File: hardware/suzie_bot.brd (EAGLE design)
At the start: 98.7 x 71.1 mm, 37 parts, among them IC1 LT1529CT33, IC2 L9637D, IC3 IC_TXB0108-TSSOP-20, U1 ATMEGA1284P-AU, Y1 14.7456, Y2 6.0, Y3 16.0

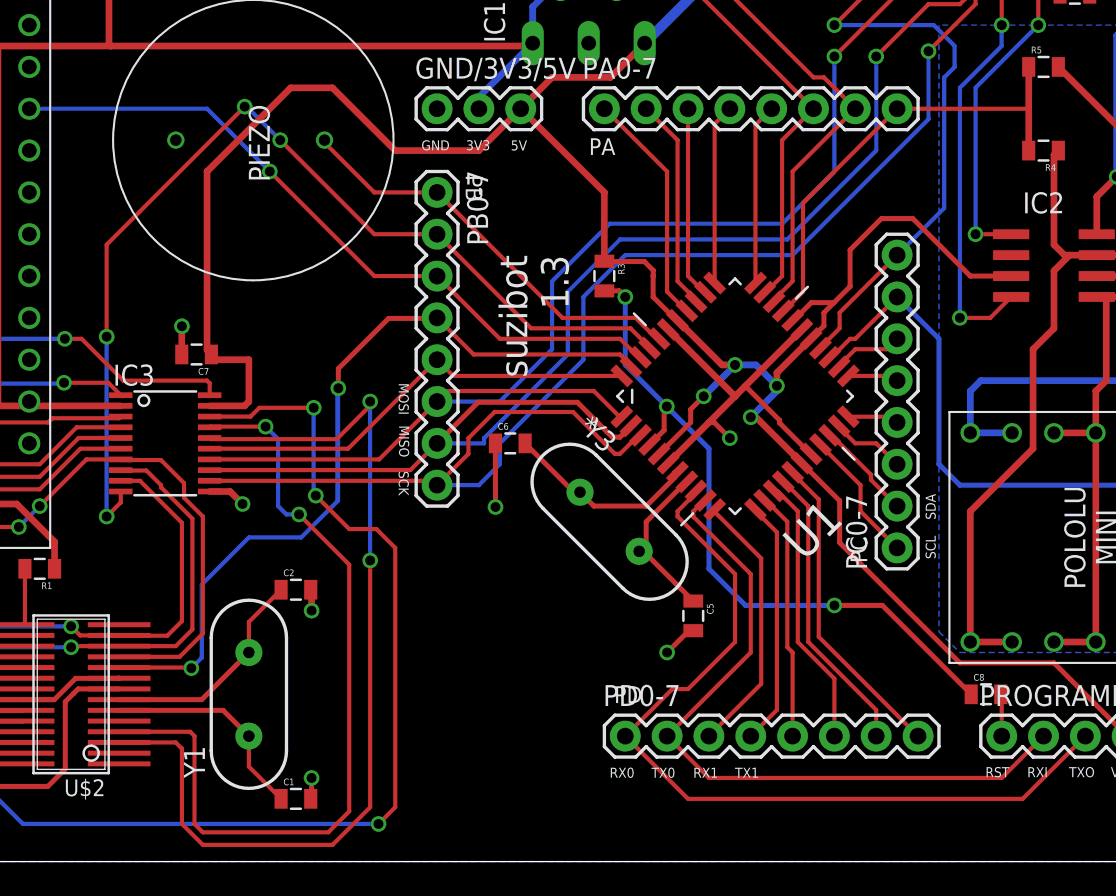
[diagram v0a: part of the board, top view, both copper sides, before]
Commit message: Adding LED to PB1 (per https://www.flickr.com/photos/maniacbug/6413368937/)
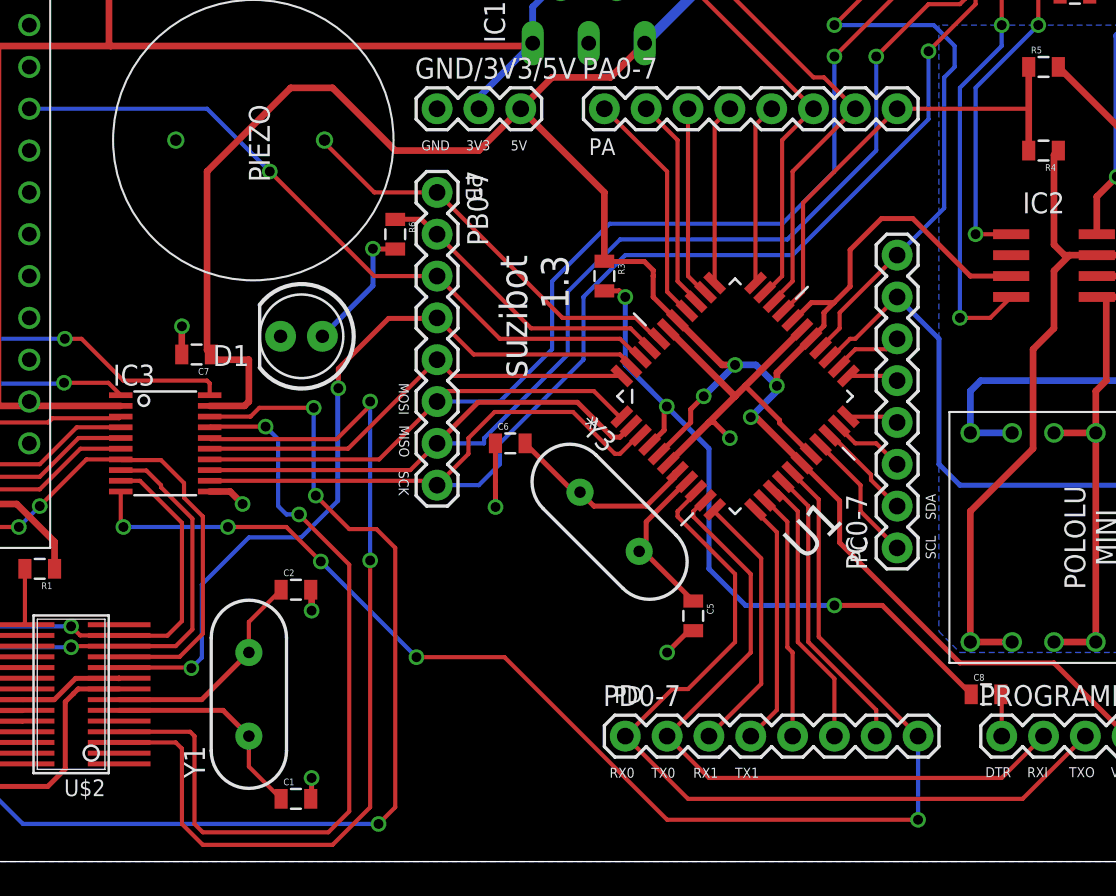
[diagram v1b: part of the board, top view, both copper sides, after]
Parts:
- added D1: RED, SparkFun-LED:LED5MM
- added R6: 330, SparkFun-Passives:0805
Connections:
- removed net PB1: IC3.10, PB0-7.2, U1.41
- new net N$2: PB0-7.2, R6.1, U1.41
- new net N$25: D1.A, R6.2
- net GND: now also D1.K
- net PD7: now also IC3.10
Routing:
- net PD7: track 19.2 -> 82.1 mm, vias 0 -> 5
- net PB1: track 60.9 -> 0.00 mm, vias 4 -> 0
- net N$2: track 0.00 -> 18.7 mm
- net N$25: track 0.00 -> 7.96 mm, vias 0 -> 1
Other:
- board text added: "DTR"
- board text removed: "RST"
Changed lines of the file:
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@@
 <layer number="21" name="tPlace" color="7" fill="1" visible="yes" active="yes"/>
 <layer number="22" name="bPlace" color="7" fill="1" visible="yes" active="yes"/>
-<layer number="23" name="tOrigins" color="15" fill="1" visible="no" active="yes"/>
+<layer number="23" name="tOrigins" color="15" fill="1" visible="yes" active="yes"/>
 <layer number="24" name="bOrigins" color="15" fill="1" visible="no" active="yes"/>
 <layer number="25" name="tNames" color="7" fill="1" visible="no" active="yes"/>
@@
 <text x="60.731259375" y="10.64594375" size="1.016" layer="21" rot="R180">PD</text>
 <text x="96.1071375" y="10.71075" size="1.016" layer="21" rot="R180">PROG</text>
-<text x="81.5558875" y="5.125053125" size="0.6096" layer="21">RST</text>
+<text x="81.5558875" y="5.125053125" size="0.6096" layer="21">DTR</text>
 <text x="84.0958875" y="5.125053125" size="0.6096" layer="21">RXI</text>
 <text x="86.6358875" y="5.125053125" size="0.6096" layer="21">TXO</text>
@@
 <element name="R5" library="SparkFun-Passives" package="0805" value="50k" x="85.09" y="48.26"/>
 <element name="U$1" library="dp_devices.v6" package="CON_MICROSD_HINGED" value="CON_MICROSDHINGED" x="7.62" y="10.16" rot="R270"/>
+<element name="D1" library="SparkFun-LED" package="LED5MM" value="RED" x="40.025459375" y="31.90121875" rot="R180"/>
+<element name="R6" library="SparkFun-Passives" package="0805" value="330" x="45.72" y="38.1" rot="R270"/>
 </elements>
 <signals>
@@
 <wire x1="26.31049375" y1="11.12883125" x2="28.94663125" y2="11.12883125" width="0.3048" layer="1"/>
 <wire x1="28.94663125" y1="11.12883125" x2="28.9528" y2="11.135" width="0.3048" layer="1"/>
+<contactref element="D1" pad="K"/>
 </signal>
 <signal name="3V3" class="1">
@@
 <wire x1="76.2" y1="45.72" x2="84.19" y2="45.72" width="0.254" layer="1"/>
 </signal>
-<signal name="PB1">
-<contactref element="U1" pad="41"/>
-<contactref element="PB0-7" pad="2"/>
-<contactref element="IC3" pad="10"/>
-<wire x1="61.166909375" y1="31.1850625" x2="61.166909375" y2="31.225590625" width="0.254" layer="1"/>
-<wire x1="61.166909375" y1="31.225590625" x2="60.0075" y2="32.385" width="0.254" layer="1"/>
-<wire x1="60.0075" y1="32.385" x2="53.975" y2="32.385" width="0.254" layer="1"/>
-<wire x1="53.975" y1="32.385" x2="48.26" y2="38.1" width="0.254" layer="1"/>
-<wire x1="29.05" y1="22.475" x2="29.05" y2="21.811" width="0.254" layer="1"/>
-<wire x1="29.05" y1="21.811" x2="28.194" y2="20.955" width="0.254" layer="1"/>
-<via x="28.194" y="20.955" extent="1-16" drill="0.6"/>
-<wire x1="28.194" y1="20.955" x2="28.194" y2="31.877" width="0.254" layer="16"/>
-<via x="28.194" y="31.877" extent="1-16" drill="0.6"/>
-<wire x1="28.194" y1="31.877" x2="28.194" y2="37.465" width="0.254" layer="1"/>
-<wire x1="28.194" y1="37.465" x2="36.576" y2="45.847" width="0.254" layer="1"/>
-<via x="36.576" y="45.847" extent="1-16" drill="0.6"/>
-<wire x1="36.576" y1="45.847" x2="36.703" y2="45.847" width="0.254" layer="16"/>
-<wire x1="36.703" y1="45.847" x2="38.735" y2="43.815" width="0.254" layer="16"/>
-<via x="38.735" y="43.815" extent="1-16" drill="0.6"/>
-<wire x1="38.735" y1="43.815" x2="44.45" y2="38.1" width="0.254" layer="1"/>
-<wire x1="44.45" y1="38.1" x2="48.26" y2="38.1" width="0.254" layer="1"/>
-</signal>
 <signal name="PB2">
 <contactref element="U1" pad="42"/>
@@
 <wire x1="71.437365625" y1="21.99475" x2="71.437365625" y2="13.652634375" width="0.254" layer="1"/>
 <wire x1="71.437365625" y1="13.652634375" x2="77.47" y2="7.62" width="0.254" layer="1"/>
+<contactref element="IC3" pad="10"/>
+<wire x1="29.05" y1="22.475" x2="29.05" y2="20.48" width="0.254" layer="1"/>
+<wire x1="29.05" y1="20.48" x2="29.21" y2="20.32" width="0.254" layer="1"/>
+<via x="29.21" y="20.32" extent="1-16" drill="0.6"/>
+<wire x1="29.21" y1="20.32" x2="35.56" y2="20.32" width="0.254" layer="16"/>
+<via x="35.56" y="20.32" extent="1-16" drill="0.6"/>
+<wire x1="35.56" y1="20.32" x2="39.1036375" y2="20.32" width="0.254" layer="1"/>
+<wire x1="39.1036375" y1="20.32" x2="41.197896875" y2="18.225740625" width="0.254" layer="1"/>
+<via x="41.197896875" y="18.225740625" extent="1-16" drill="0.6"/>
+<wire x1="41.197896875" y1="18.225740625" x2="41.197896875" y2="18.22459375" width="0.254" layer="16"/>
+<wire x1="41.197896875" y1="18.22459375" x2="47.00785625" y2="12.414634375" width="0.254" layer="16"/>
+<via x="47.00785625" y="12.414634375" extent="1-16" drill="0.6"/>
+<wire x1="47.00785625" y1="12.414634375" x2="52.355365625" y2="12.414634375" width="0.254" layer="1"/>
+<wire x1="52.355365625" y1="12.414634375" x2="62.23" y2="2.54" width="0.254" layer="1"/>
+<wire x1="62.23" y1="2.54" x2="77.47" y2="2.54" width="0.254" layer="1"/>
+<via x="77.47" y="2.54" extent="1-16" drill="0.6"/>
+<wire x1="77.47" y1="2.54" x2="77.47" y2="7.62" width="0.254" layer="16"/>
 </signal>
 <signal name="PC6">
@@
 <wire x1="62.23" y1="41.91" x2="58.42" y2="45.72" width="0.254" layer="1"/>
 </signal>
+<signal name="N$2">
+<contactref element="U1" pad="41"/>
+<contactref element="PB0-7" pad="2"/>
+<wire x1="61.166909375" y1="31.1850625" x2="61.166909375" y2="31.225590625" width="0.254" layer="1"/>
+<wire x1="61.166909375" y1="31.225590625" x2="60.0075" y2="32.385" width="0.254" layer="1"/>
+<wire x1="60.0075" y1="32.385" x2="53.975" y2="32.385" width="0.254" layer="1"/>
+<wire x1="53.975" y1="32.385" x2="48.26" y2="38.1" width="0.254" layer="1"/>
+<contactref element="R6" pad="1"/>
+<wire x1="48.26" y1="38.1" x2="48.214775" y2="38.1" width="0.3048" layer="1"/>
+<wire x1="48.214775" y1="38.1" x2="47.305378125" y2="39.009396875" width="0.3048" layer="1"/>
+<wire x1="47.305378125" y1="39.009396875" x2="45.729396875" y2="39.009396875" width="0.3048" layer="1"/>
+<wire x1="45.729396875" y1="39.009396875" x2="45.72" y2="39" width="0.3048" layer="1"/>
+</signal>
+<signal name="N$25">
+<contactref element="D1" pad="A"/>
+<contactref element="R6" pad="2"/>
+<wire x1="45.72" y1="37.2" x2="44.38378125" y2="37.2" width="0.3048" layer="1"/>
+<wire x1="44.38378125" y1="37.2" x2="44.36254375" y2="37.2212375" width="0.3048" layer="1"/>
+<via x="44.36254375" y="37.2212375" extent="1-16" drill="0.6"/>
+<wire x1="44.36254375" y1="37.2212375" x2="44.36254375" y2="34.968303125" width="0.3048" layer="16"/>
+<wire x1="44.36254375" y1="34.968303125" x2="41.295459375" y2="31.90121875" width="0.3048" layer="16"/>
+</signal>
 </signals>

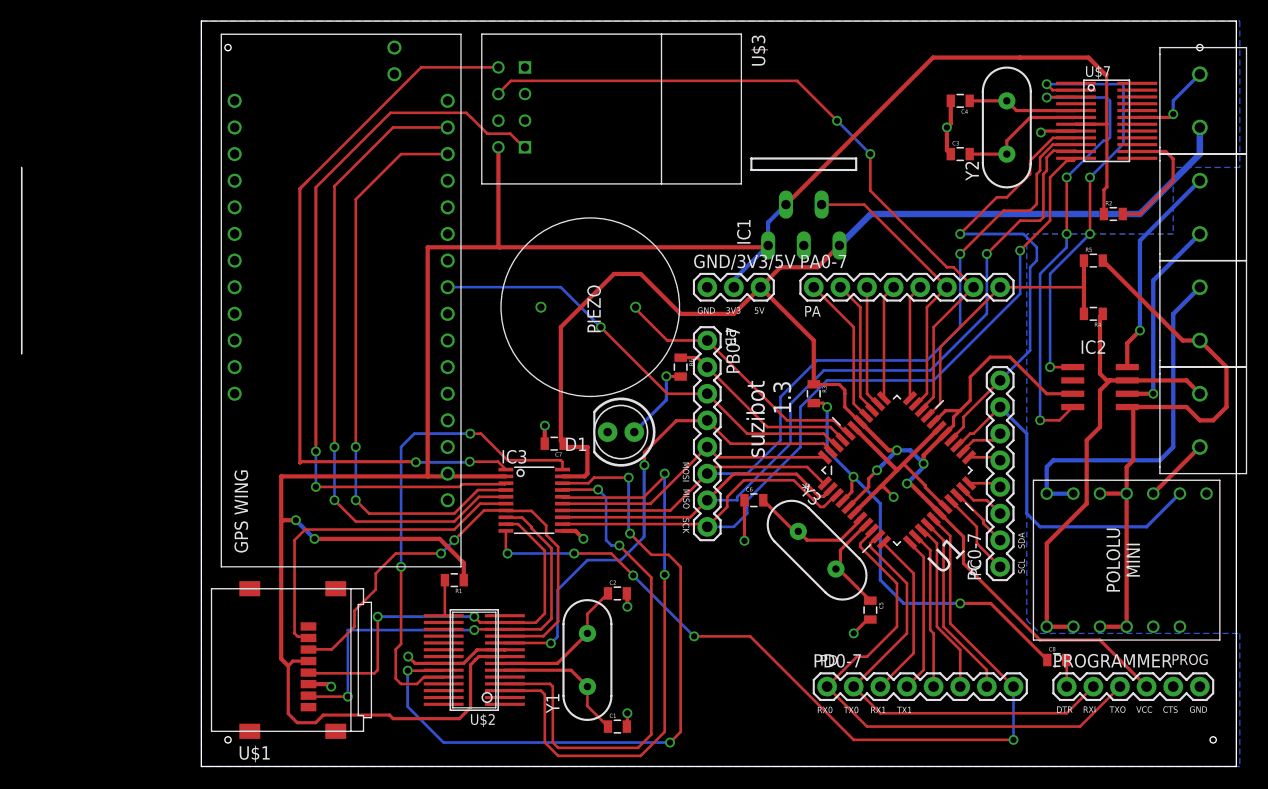
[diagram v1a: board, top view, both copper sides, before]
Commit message: Updating to v1.3 boardfile (what was once an atmega328p is now an atmega1284p)
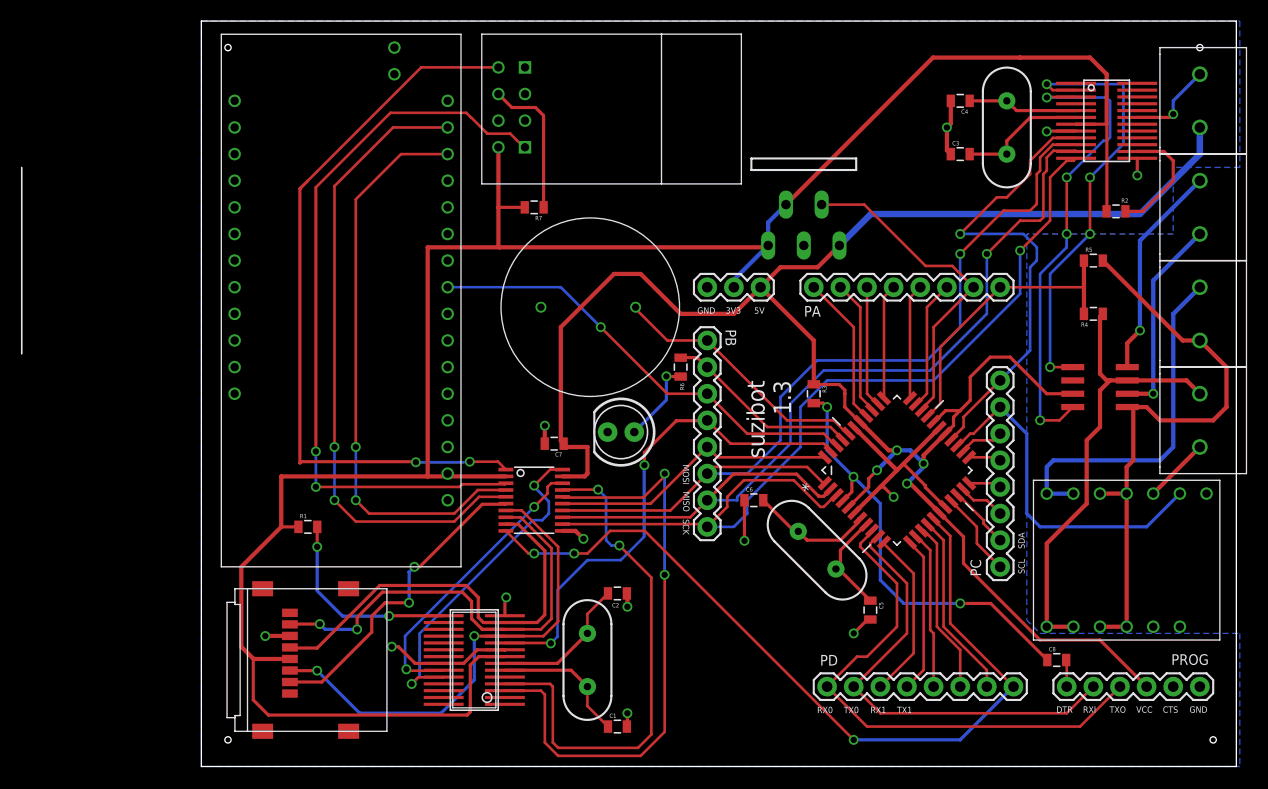
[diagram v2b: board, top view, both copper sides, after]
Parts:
- added R7: 1k, SparkFun-Passives:0805
- R4: value 70k -> 33k
- R5: value 50k -> 12k
- moved R1 14.9 mm to (10.2, 22.9), turned to 0 degrees
- moved U$1 3.43 mm to (11.0, 10.2), turned to 90 degrees
- moved R2 0.36 mm to (87.2, 53.0)
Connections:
- removed net PA5: IC1.4, PA0-7.6, U1.32
- new net N$28: PA0-7.6, U1.32
- new net N$4: R7.1, U$3.CH_PD
- net 12V-OUT: now also IC2.VS; no longer IC2.7
- net 3V3: now also IC3.VCCA, R7.2, U$1.VDD, U$2.VDD, U$7.VDD; no longer IC3.2, U$1.4, U$2.8, U$7.7
- net 5V: now also IC2.VCC, IC3.VCCB; no longer IC2.3, IC3.19
- net EXTGND: now also IC2.GND; no longer IC2.5
- net GND: now also IC3.GND, U$1.VSS, U$2.I2C/!SPI, U$2.SDA/VSS, U$2.VSS, U$7.I2C/!SPI, U$7.SDA/VSS, U$7.VSS; no longer IC3.11, U$1.6, U$2.22, U$2.9, U$7.19, U$7.8
- net K: now also IC2.K; no longer IC2.6
- net L: now also IC2.LI; no longer IC2.8
- net MISO3V3: now also IC3.A7, U$1.DAT0/DO, U$2.-/SO; no longer IC3.8, U$1.7, U$2.12
- net MOSI3V3: now also IC3.A6, U$1.CMD/DI, U$2.A1/SI; no longer IC3.7, U$1.3, U$2.11
- net N$1: now also U$2.XTAL1; no longer U$2.6
- net N$11: now also IC3.B1, U$2.RXB; no longer IC3.20, U$2.24
- net N$12: now also IC3.B2, U$2.TXB; no longer IC3.18, U$2.23
- net N$14: now also IC3.A4; no longer IC3.5
- net N$15: now also IC2.RX, U$7.TX; no longer IC2.1, U$7.2
- net N$16: now also U$7.!IRQ; no longer U$7.14
- net N$17: now also IC3.B3, U$2.RXA; no longer IC3.17, U$2.4
- net N$18: now also U$2.!IRQ; no longer U$2.15
- net N$19: now also IC2.TX, U$7.RX; no longer IC2.4, U$7.3
- net N$20: now also U$7.XTAL1; no longer U$7.5
- net N$21: now also U$7.XTAL2; no longer U$7.6
- net N$22: now also IC3.A3; no longer IC3.4
- net N$23: now also IC3.B4, U$2.TXA; no longer IC3.16, U$2.3
- net N$24: now also IC3.A5, U$1.DAT3/CS; no longer IC3.6, U$1.2
- net N$26: now also IC3.B5; no longer IC3.15
- net N$3: now also U$2.XTAL2; no longer U$2.7
- net N$5: now also IC3.A1; no longer IC3.1
- net N$8: now also IC3.A2; no longer IC3.3
- net PA6: now also IC1.4; no longer U$3.CH_PD
- net PB3: now also U$2.A0/!CS; no longer U$2.10
- net PB5/MOSI: now also IC3.B6, U$7.A1/SI; no longer IC3.14, U$7.10
- net PB6/MISO: now also IC3.B7, U$7.-/SO; no longer IC3.13, U$7.11
- net PB7/SCLK: now also IC3.B8, U$7.SCL/SCLK; no longer IC3.12, U$7.12
- net PC7: now also U$7.A0/!CS; no longer U$7.9
- net PD7: now also IC3.OE; no longer IC3.10
- net SKCK3V3: now also IC3.A8, U$1.SCLK, U$2.SCL/SCLK; no longer IC3.9, U$1.5, U$2.13
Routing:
- net N$12: track 68.6 -> 28.3 mm, vias 4 -> 2
- net PA6: track 69.8 -> 31.5 mm, vias 2 -> 0
- net PA5: track 27.6 -> 0.00 mm
- net N$18: track 3.44 -> 19.2 mm, vias 0 -> 2
- net N$4: track 0.00 -> 13.9 mm
- net N$11: track 45.1 -> 32.1 mm
- net N$28: track 0.00 -> 12.4 mm
- net 3V3: track 221.3 -> 209.4 mm, vias 2 -> 0
- net GND: track 66.9 -> 71.8 mm, vias 12 -> 14
- net PD7: track 82.1 -> 79.7 mm, vias 5 -> 3
- net N$24: track 32.3 -> 30.3 mm, vias 0 -> 2
- net SKCK3V3: track 39.1 -> 40.6 mm, vias 2 -> 0
- net MOSI3V3: track 45.8 -> 47.0 mm
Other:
- board text added: "17 October 2016"
- board text removed: "16 October 2016"
